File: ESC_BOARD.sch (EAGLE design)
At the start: 34 parts, among them J1 TE_2351886-3-(VERT), J2 TE_2351886-3-(VERT), J3 TE_2351886-3-(VERT), J4 TE_2351886-3-(VERT), Y1 ECS-80-S-4X

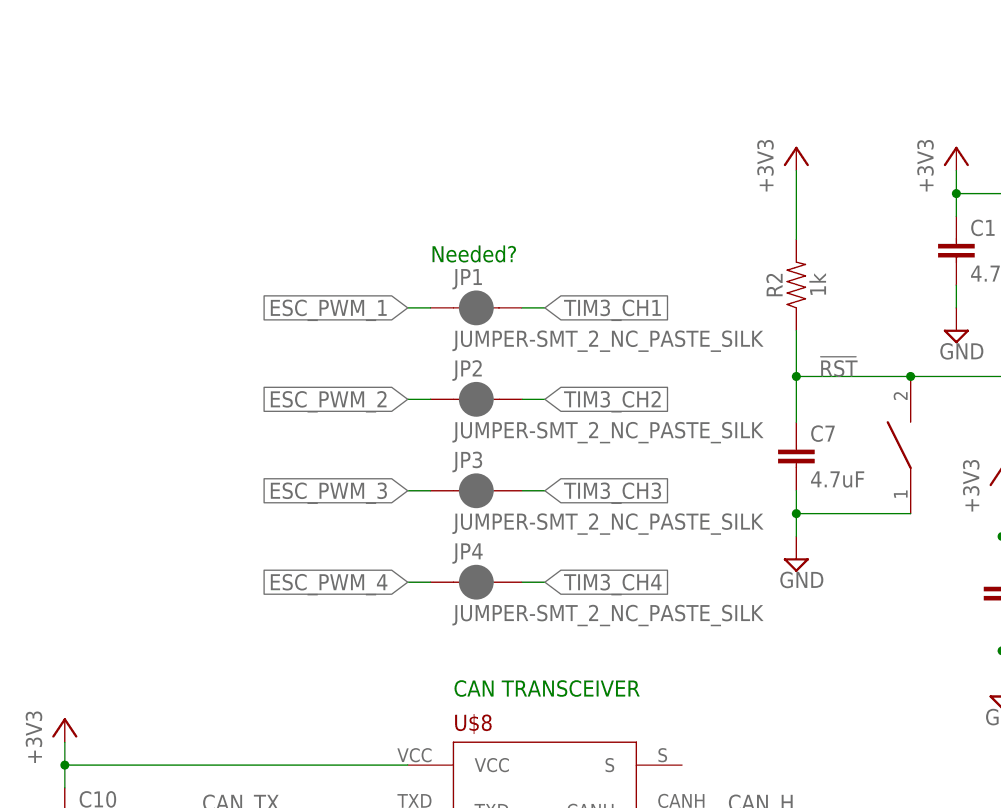
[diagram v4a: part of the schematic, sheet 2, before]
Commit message: added pins for programing ESCs
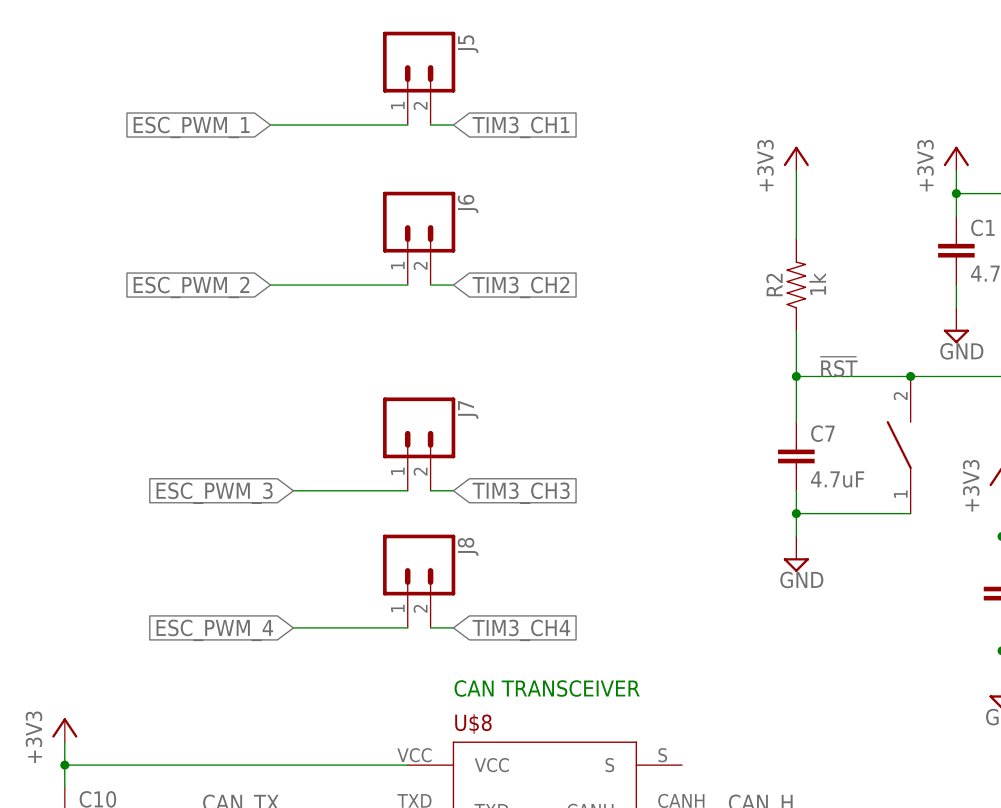
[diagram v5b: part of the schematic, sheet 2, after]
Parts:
- removed JP1, JP2, JP3, JP4: JUMPER-SMT_2_NC_PASTE_SILK, SparkFun-Jumpers:JUMPER-SMT_2_NC_PASTE_SILK
- added J5, J6, J7, J8: (no value), SparkFun-Connectors:CONN_02
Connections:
- net ESC_PWM_1: now also J5.1; no longer JP1.1
- net ESC_PWM_2: now also J6.1; no longer JP2.1
- net ESC_PWM_3: now also J7.1; no longer JP3.1
- net ESC_PWM_4: now also J8.1; no longer JP4.1
- net TIM3_CH1: now also J5.2; no longer JP1.2
- net TIM3_CH2: now also J6.2; no longer JP2.2
- net TIM3_CH3: now also J7.2; no longer JP3.2
- net TIM3_CH4: now also J8.2; no longer JP4.2
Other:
- note removed: "Needed?"
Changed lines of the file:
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@@
 <part name="GND15" library="supply2" library_urn="urn:adsk.eagle:library:372" deviceset="GND" device=""/>
 <part name="FRAME1" library="frames" library_urn="urn:adsk.eagle:library:229" deviceset="A4L-LOC" device=""/>
-<part name="JP1" library="SparkFun-Jumpers" library_urn="urn:adsk.eagle:library:528" deviceset="JUMPER-SMT_2_NC_PASTE" device="_SILK" package3d_urn="urn:adsk.eagle:package:39282/1"/>
-<part name="JP2" library="SparkFun-Jumpers" library_urn="urn:adsk.eagle:library:528" deviceset="JUMPER-SMT_2_NC_PASTE" device="_SILK" package3d_urn="urn:adsk.eagle:package:39282/1"/>
-<part name="JP3" library="SparkFun-Jumpers" library_urn="urn:adsk.eagle:library:528" deviceset="JUMPER-SMT_2_NC_PASTE" device="_SILK" package3d_urn="urn:adsk.eagle:package:39282/1"/>
-<part name="JP4" library="SparkFun-Jumpers" library_urn="urn:adsk.eagle:library:528" deviceset="JUMPER-SMT_2_NC_PASTE" device="_SILK" package3d_urn="urn:adsk.eagle:package:39282/1"/>
 <part name="R4" library="SparkFun-Resistors" library_urn="urn:adsk.eagle:library:532" deviceset="1KOHM" device="-0603-1/10W-1%" package3d_urn="urn:adsk.eagle:package:39650/1" value="1k"/>
 <part name="U$2" library="MURATA_3pin_dcdc" deviceset="MURATA-DC-DC" device="" package3d_urn="urn:adsk.eagle:package:23169699/2"/>
@@
 <part name="J3" library="TE 3 pin 3.5mm" deviceset="TE_2351886-3-(VERT)" device="" package3d_urn="urn:adsk.eagle:package:24331182/2"/>
 <part name="J4" library="TE 3 pin 3.5mm" deviceset="TE_2351886-3-(VERT)" device="" package3d_urn="urn:adsk.eagle:package:24331182/2"/>
+<part name="J5" library="SparkFun-Connectors" library_urn="urn:adsk.eagle:library:513" deviceset="CONN_02" device="" package3d_urn="urn:adsk.eagle:package:38039/1"/>
+<part name="J6" library="SparkFun-Connectors" library_urn="urn:adsk.eagle:library:513" deviceset="CONN_02" device="" package3d_urn="urn:adsk.eagle:package:38039/1"/>
+<part name="J7" library="SparkFun-Connectors" library_urn="urn:adsk.eagle:library:513" deviceset="CONN_02" device="" package3d_urn="urn:adsk.eagle:package:38039/1"/>
+<part name="J8" library="SparkFun-Connectors" library_urn="urn:adsk.eagle:library:513" deviceset="CONN_02" device="" package3d_urn="urn:adsk.eagle:package:38039/1"/>
 </parts>
 <sheets>
@@
 <text x="175.26" y="86.36" size="1.778" layer="91">OSCILLATOR</text>
 <text x="157.48" y="165.1" size="1.778" layer="91">STM32F042K6T6</text>
-<text x="60.96" y="144.78" size="1.778" layer="91">Needed?</text>
 </plain>
 <instances>
@@
 <attribute name="NAME" x="26.67" y="61.722" size="1.778" layer="95"/>
 </instance>
-<instance part="JP1" gate="G$1" x="66.04" y="139.7" smashed="yes">
-<attribute name="NAME" x="63.5" y="142.24" size="1.778" layer="95" font="vector"/>
-<attribute name="VALUE" x="63.5" y="137.16" size="1.778" layer="96" font="vector" align="top-left"/>
-</instance>
-<instance part="JP2" gate="G$1" x="66.04" y="129.54" smashed="yes">
-<attribute name="NAME" x="63.5" y="132.08" size="1.778" layer="95" font="vector"/>
-<attribute name="VALUE" x="63.5" y="127" size="1.778" layer="96" font="vector" align="top-left"/>
-</instance>
-<instance part="JP3" gate="G$1" x="66.04" y="119.38" smashed="yes">
-<attribute name="NAME" x="63.5" y="121.92" size="1.778" layer="95" font="vector"/>
-<attribute name="VALUE" x="63.5" y="116.84" size="1.778" layer="96" font="vector" align="top-left"/>
-</instance>
-<instance part="JP4" gate="G$1" x="66.04" y="109.22" smashed="yes">
-<attribute name="NAME" x="63.5" y="111.76" size="1.778" layer="95" font="vector"/>
-<attribute name="VALUE" x="63.5" y="106.68" size="1.778" layer="96" font="vector" align="top-left"/>
-</instance>
 <instance part="R4" gate="G$1" x="132.08" y="68.58" smashed="yes" rot="R90">
 <attribute name="NAME" x="130.556" y="68.58" size="1.778" layer="95" font="vector" rot="R90" align="bottom-center"/>
@@
 <attribute name="NAME" x="189.611" y="157.988" size="1.778" layer="95" font="vector" rot="R90"/>
 <attribute name="VALUE" x="194.945" y="157.988" size="1.778" layer="96" font="vector" rot="R90" align="top-left"/>
+</instance>
+<instance part="J5" gate="G$1" x="58.42" y="167.64" smashed="yes" rot="R270">
+<attribute name="VALUE" x="53.594" y="170.18" size="1.778" layer="96" font="vector" rot="R270"/>
+<attribute name="NAME" x="64.008" y="170.18" size="1.778" layer="95" font="vector" rot="R270"/>
+</instance>
+<instance part="J6" gate="G$1" x="58.42" y="149.86" smashed="yes" rot="R270">
+<attribute name="VALUE" x="53.594" y="152.4" size="1.778" layer="96" font="vector" rot="R270"/>
+<attribute name="NAME" x="64.008" y="152.4" size="1.778" layer="95" font="vector" rot="R270"/>
+</instance>
+<instance part="J7" gate="G$1" x="58.42" y="127" smashed="yes" rot="R270">
+<attribute name="VALUE" x="53.594" y="129.54" size="1.778" layer="96" font="vector" rot="R270"/>
+<attribute name="NAME" x="64.008" y="129.54" size="1.778" layer="95" font="vector" rot="R270"/>
+</instance>
+<instance part="J8" gate="G$1" x="58.42" y="111.76" smashed="yes" rot="R270">
+<attribute name="VALUE" x="53.594" y="114.3" size="1.778" layer="96" font="vector" rot="R270"/>
+<attribute name="NAME" x="64.008" y="114.3" size="1.778" layer="95" font="vector" rot="R270"/>
 </instance>
 </instances>
@@
 <net name="TIM3_CH1" class="1">
 <segment>
-<pinref part="JP1" gate="G$1" pin="2"/>
-<wire x1="71.12" y1="139.7" x2="73.66" y2="139.7" width="0.1524" layer="91"/>
-<label x="73.66" y="139.7" size="1.778" layer="95" xref="yes"/>
+<wire x1="60.96" y1="160.02" x2="63.5" y2="160.02" width="0.1524" layer="91"/>
+<label x="63.5" y="160.02" size="1.778" layer="95" xref="yes"/>
+<pinref part="J5" gate="G$1" pin="2"/>
 </segment>
 <segment>
@@
 <net name="TIM3_CH2" class="1">
 <segment>
-<pinref part="JP2" gate="G$1" pin="2"/>
-<wire x1="71.12" y1="129.54" x2="73.66" y2="129.54" width="0.1524" layer="91"/>
-<label x="73.66" y="129.54" size="1.778" layer="95" xref="yes"/>
+<wire x1="60.96" y1="142.24" x2="63.5" y2="142.24" width="0.1524" layer="91"/>
+<label x="63.5" y="142.24" size="1.778" layer="95" xref="yes"/>
+<pinref part="J6" gate="G$1" pin="2"/>
 </segment>
 <segment>
@@
 <net name="TIM3_CH3" class="1">
 <segment>
-<pinref part="JP3" gate="G$1" pin="2"/>
-<wire x1="71.12" y1="119.38" x2="73.66" y2="119.38" width="0.1524" layer="91"/>
-<label x="73.66" y="119.38" size="1.778" layer="95" xref="yes"/>
+<wire x1="60.96" y1="119.38" x2="63.5" y2="119.38" width="0.1524" layer="91"/>
+<label x="63.5" y="119.38" size="1.778" layer="95" xref="yes"/>
+<pinref part="J7" gate="G$1" pin="2"/>
 </segment>
 <segment>
@@
 <net name="TIM3_CH4" class="1">
 <segment>
-<pinref part="JP4" gate="G$1" pin="2"/>
-<wire x1="71.12" y1="109.22" x2="73.66" y2="109.22" width="0.1524" layer="91"/>
-<label x="73.66" y="109.22" size="1.778" layer="95" xref="yes"/>
+<wire x1="60.96" y1="104.14" x2="63.5" y2="104.14" width="0.1524" layer="91"/>
+<label x="63.5" y="104.14" size="1.778" layer="95" xref="yes"/>
+<pinref part="J8" gate="G$1" pin="2"/>
 </segment>
 <segment>
@@
 <net name="ESC_PWM_1" class="1">
 <segment>
-<pinref part="JP1" gate="G$1" pin="1"/>
-<wire x1="60.96" y1="139.7" x2="58.42" y2="139.7" width="0.1524" layer="91"/>
-<label x="58.42" y="139.7" size="1.778" layer="95" rot="R180" xref="yes"/>
+<wire x1="58.42" y1="160.02" x2="43.18" y2="160.02" width="0.1524" layer="91"/>
+<label x="43.18" y="160.02" size="1.778" layer="95" rot="R180" xref="yes"/>
+<pinref part="J5" gate="G$1" pin="1"/>
 </segment>
 </net>
 <net name="ESC_PWM_2" class="1">
 <segment>
-<pinref part="JP2" gate="G$1" pin="1"/>
-<wire x1="60.96" y1="129.54" x2="58.42" y2="129.54" width="0.1524" layer="91"/>
-<label x="58.42" y="129.54" size="1.778" layer="95" rot="R180" xref="yes"/>
+<wire x1="58.42" y1="142.24" x2="43.18" y2="142.24" width="0.1524" layer="91"/>
+<label x="43.18" y="142.24" size="1.778" layer="95" rot="R180" xref="yes"/>
+<pinref part="J6" gate="G$1" pin="1"/>
 </segment>
 </net>
 <net name="ESC_PWM_3" class="1">
 <segment>
-<pinref part="JP3" gate="G$1" pin="1"/>
-<wire x1="60.96" y1="119.38" x2="58.42" y2="119.38" width="0.1524" layer="91"/>
-<label x="58.42" y="119.38" size="1.778" layer="95" rot="R180" xref="yes"/>
+<wire x1="58.42" y1="119.38" x2="45.72" y2="119.38" width="0.1524" layer="91"/>
+<label x="45.72" y="119.38" size="1.778" layer="95" rot="R180" xref="yes"/>
+<pinref part="J7" gate="G$1" pin="1"/>
 </segment>
 </net>
 <net name="ESC_PWM_4" class="1">
 <segment>
-<pinref part="JP4" gate="G$1" pin="1"/>
-<wire x1="60.96" y1="109.22" x2="58.42" y2="109.22" width="0.1524" layer="91"/>
-<label x="58.42" y="109.22" size="1.778" layer="95" rot="R180" xref="yes"/>
-</segment>
-</net>
+<wire x1="58.42" y1="104.14" x2="45.72" y2="104.14" width="0.1524" layer="91"/>
+<label x="45.72" y="104.14" size="1.778" layer="95" rot="R180" xref="yes"/>
+<pinref part="J8" gate="G$1" pin="1"/>
+</segment>
+</net>
